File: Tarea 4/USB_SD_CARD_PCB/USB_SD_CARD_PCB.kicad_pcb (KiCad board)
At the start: 2 copper layers, 54.8 x 37.1 mm, 3 parts

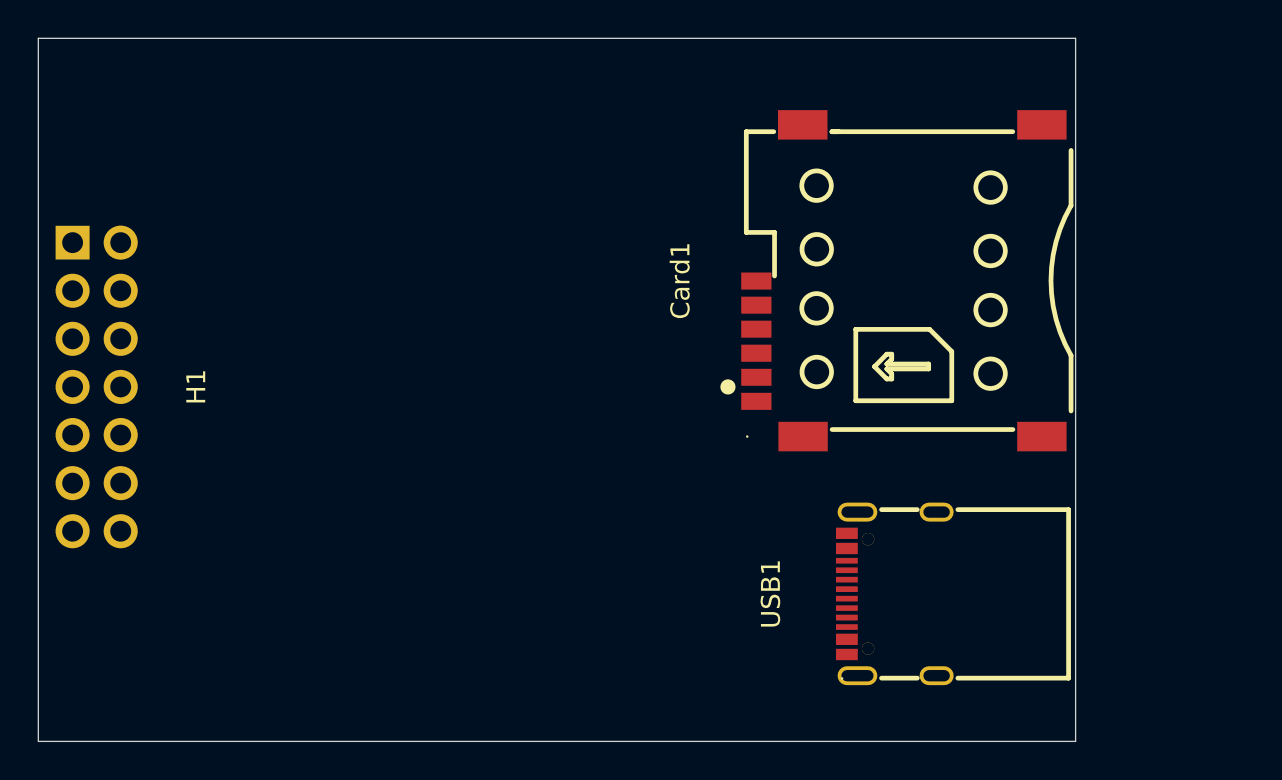
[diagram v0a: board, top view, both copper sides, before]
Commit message: USB type c Conexiones
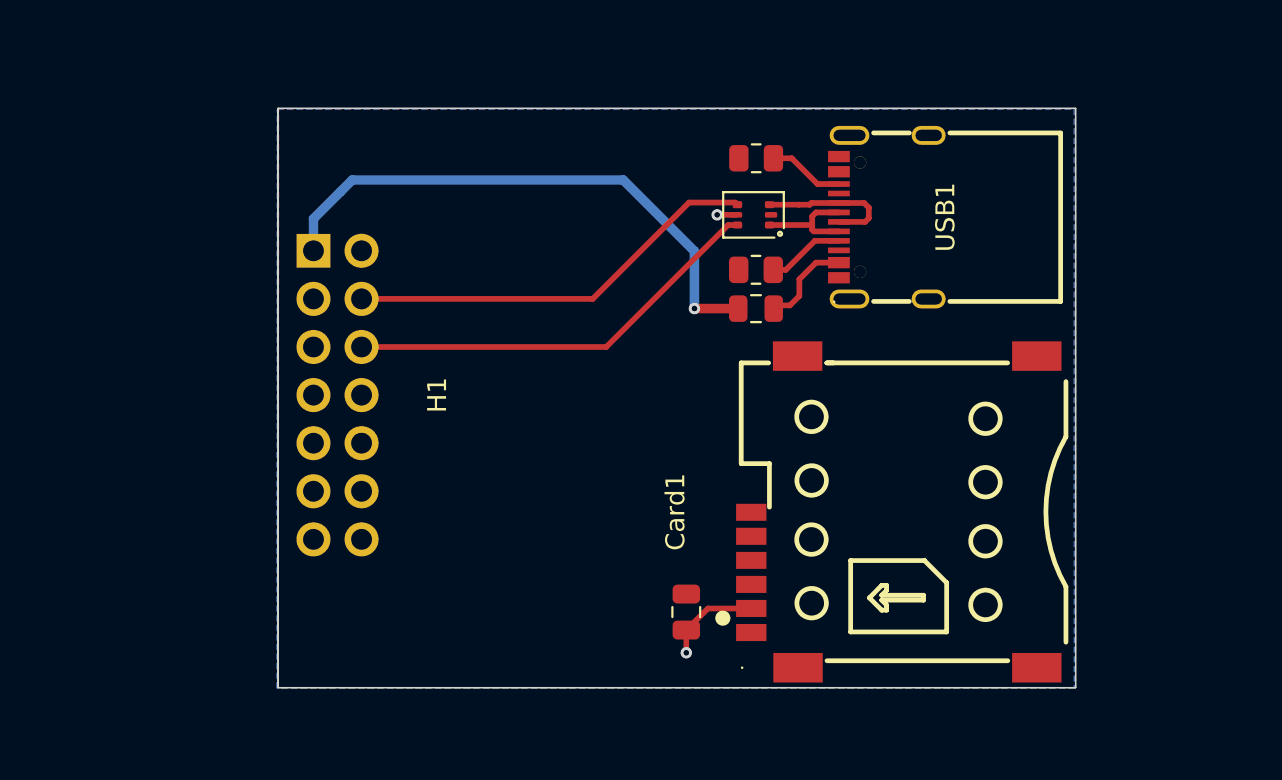
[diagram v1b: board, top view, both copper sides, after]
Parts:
- added C3: 100nf, Capacitor_SMD:C_0805_2012Metric, F.Cu at (111.8, 95.1)
- added D1: USBLC6-2P6, PCM_Package_TO_SOT_SMD_AKL:SOT-666, F.Cu at (115.3, 74.2)
- added F1: Polyfuse_Small, Fuse:Fuse_0805_2012Metric, F.Cu at (115.5, 79.1)
- added R1: 5.1k, Resistor_SMD:R_0805_2012Metric, F.Cu at (115.5, 77.1)
- added R2: 5.1k, Resistor_SMD:R_0805_2012Metric, F.Cu at (115.5, 71.2)
- moved USB1 19.9 mm to (122.2, 74.3)
- moved H1 12.7 mm to (93.4, 83.7)
- moved Card1 12.2 mm to (122.8, 89.8)
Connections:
- Card1 pad 10: unconnected-(Card1-GND-Pad10) -> GND
- Card1 pad 7: unconnected-(Card1-GND-Pad7) -> GND
- Card1 pad 8: unconnected-(Card1-GND-Pad8) -> GND
- Card1 pad 9: unconnected-(Card1-GND-Pad9) -> GND
- Card1 pad C1: unconnected-(Card1-VCC-PadC1) -> +3.3V
- Card1 pad C3: unconnected-(Card1-CLK-PadC3) -> /clk
- Card1 pad C5: unconnected-(Card1-GND-PadC5) -> GND
- Card1 pad C7: unconnected-(Card1-I/O-PadC7) -> /GPIO1
- H1 pad 1: unconnected-(H1-Pad1) -> +5V
- H1 pad 10: unconnected-(H1-Pad10) -> /i2c_scl
- H1 pad 11: unconnected-(H1-Pad11) -> /GPIO1
- H1 pad 12: unconnected-(H1-Pad12) -> /GPIO2
- H1 pad 13: unconnected-(H1-Pad13) -> GND
- H1 pad 14: unconnected-(H1-Pad14) -> GND
- H1 pad 2: unconnected-(H1-Pad2) -> +3.3V
- H1 pad 3: unconnected-(H1-Pad3) -> /cs
- H1 pad 4: unconnected-(H1-Pad4) -> /usb+
- H1 pad 5: unconnected-(H1-Pad5) -> /mosi
- H1 pad 6: unconnected-(H1-Pad6) -> /usb-
- H1 pad 7: unconnected-(H1-Pad7) -> /miso
- H1 pad 8: unconnected-(H1-Pad8) -> /i2c_sda
- H1 pad 9: unconnected-(H1-Pad9) -> /clk
- USB1 pad A5: unconnected-(USB1-CC1-PadA5) -> Net-(USB1-CC1)
- USB1 pad A6: unconnected-(USB1-DP1-PadA6) -> /D+
- USB1 pad A7: unconnected-(USB1-DN1-PadA7) -> /D-
- USB1 pad B5: unconnected-(USB1-CC2-PadB5) -> Net-(USB1-CC2)
- USB1 pad B6: unconnected-(USB1-DP2-PadB6) -> /D+
- USB1 pad B7: unconnected-(USB1-DN2-PadB7) -> /D-
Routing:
- net +5V: track 0.00 -> 29.6 mm, vias 0 -> 1
- net /usb-: track 0.00 -> 22.5 mm
- net /usb+: track 0.00 -> 22.0 mm
- net /D+: track 0.00 -> 7.59 mm
- net +3.3V: track 0.00 -> 6.10 mm, vias 0 -> 2
- net /D-: track 0.00 -> 5.92 mm
- net Net-(F1-Pad2): track 0.00 -> 4.96 mm
- net Net-(USB1-CC1): track 0.00 -> 4.10 mm
- net Net-(USB1-CC2): track 0.00 -> 4.02 mm
- added copper zone on B.Cu, net +3.3V
- added copper zone on F.Cu, net GND
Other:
- board size 54.8 x 37.1 mm -> 42.1 x 30.6 mm

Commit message: USB CARD Y SD
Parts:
- removed Card1: SMC-202-6, EasyEDA:SIM-SMD_SMC-202-6
- removed H1: PZ254R-12-14P, EasyEDA:HDR-TH_14P-P2.54-H-M-R2-C7-S2.54
- added C1: 100nf, Capacitor_SMD:C_0805_2012Metric, F.Cu at (118.0, 82.8)
- added Card2: TF-115, EasyEDA:TF-SMD_TF-115, F.Cu at (128.8, 89.3)
- added FPC1: FPC-05FB-30PH20, EasyEDA:FPC-SMD_30P-P0.50_FPC-05FB-30PH20, F.Cu at (109.1, 84.0)
- added J1: PZ254R-12-16P, EasyEDA:HDR-TH_16P-P2.54-H-M-R2-C8-S2.54, F.Cu at (99.1, 84.1)
- added R3: 10k, Resistor_SMD:R_0805_2012Metric, F.Cu at (118.0, 85.1)
- added R4: 10k, Resistor_SMD:R_0805_2012Metric, F.Cu at (118.0, 88.1)
- added R5: 10k, Resistor_SMD:R_0805_2012Metric, F.Cu at (118.0, 91.0)
- added R6: 10k, Resistor_SMD:R_0805_2012Metric, F.Cu at (118.0, 94.0)
- moved USB1 7.49 mm to (129.7, 74.2)
- moved R1 6.91 mm to (122.3, 76.0)
- moved F1 6.91 mm to (122.3, 78.0)
- moved R2 6.91 mm to (122.3, 70.1)
- moved D1 6.91 mm to (122.2, 73.1)
- moved C3 6.43 mm to (118.1, 96.5), turned to 0 degrees
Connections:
- D1 pad 4: /usb+ -> /USB+
- D1 pad 6: /usb- -> /USB-
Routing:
- net +5V: track 29.6 -> 0.00 mm, vias 1 -> 0
- net /usb-: track 22.5 -> 0.00 mm
- net /usb+: track 22.0 -> 0.00 mm
- net /D+: track 7.59 -> 0.00 mm
- net +3.3V: track 6.10 -> 0.00 mm, vias 2 -> 0
- net /D-: track 5.92 -> 0.00 mm
- net Net-(F1-Pad2): track 4.96 -> 0.00 mm
- net Net-(USB1-CC1): track 4.10 -> 0.00 mm
- net Net-(USB1-CC2): track 4.02 -> 0.00 mm
- removed copper zone on B.Cu, net +3.3V
- removed copper zone on F.Cu, net GND
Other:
- board size 42.1 x 30.6 mm -> 42.4 x 32.3 mm
- copper layers 2 -> 4

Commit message: Actualizacion 18/04/26
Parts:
- added C2: 10uF, Capacitor_SMD:C_0201_0603Metric, F.Cu at (113.6, 93.0)
- added R10: 10K, PCM_Resistor_SMD_AKL:R_0603_1608Metric, F.Cu at (115.5, 91.0)
- added R11: 10K, PCM_Resistor_SMD_AKL:R_0603_1608Metric, F.Cu at (115.5, 89.1)
- added R7: 6.8K, PCM_Resistor_SMD_AKL:R_0603_1608Metric, F.Cu at (116.0, 97.2)
- added R8: 300R, PCM_Resistor_SMD_AKL:R_0603_1608Metric, F.Cu at (112.2, 95.4)
- added R9: 10K, PCM_Resistor_SMD_AKL:R_0603_1608Metric, F.Cu at (115.5, 87.1)
- added U1: MT9700-N, EasyEDA:SOT-23-5_L2.9-W1.6-P0.95-LS2.9-BL, F.Cu at (116.0, 94.3)
- R3, R4, R5, R6: footprint Resistor_SMD:R_0805_2012Metric -> PCM_Resistor_SMD_AKL:R_0603_1608Metric
- moved C3 28.1 mm to (126.1, 69.6)
- moved R5 5.03 mm to (120.3, 95.5)
- moved D1 4.26 mm to (126.3, 74.0)
- moved R2 4.21 mm to (126.2, 71.6)
- moved F1 4.07 mm to (126.3, 78.4)
- moved R1 4.07 mm to (126.3, 76.3)
- moved C1 2.48 mm to (120.3, 82.1)
- moved R3 2.48 mm to (120.4, 84.4)
- moved R4 2.48 mm to (120.4, 87.4)
- moved R6 2.30 mm to (120.3, 93.7)
- moved USB1 2.10 mm to (131.8, 74.3)
- moved Card2 1.92 mm to (130.7, 89.2)
- moved FPC1 0.95 mm to (110.0, 84.0), turned to -90 degrees
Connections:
- FPC1 pad 1: unconnected-(FPC1-Pad1) -> GND
- FPC1 pad 2: unconnected-(FPC1-Pad2) -> VDD
- FPC1 pad 20: unconnected-(FPC1-Pad20) -> /LED+
- FPC1 pad 21: unconnected-(FPC1-Pad21) -> GND
- FPC1 pad 22: unconnected-(FPC1-Pad22) -> GND
- FPC1 pad 23: unconnected-(FPC1-Pad23) -> GND
- FPC1 pad 24: unconnected-(FPC1-Pad24) -> GND
- FPC1 pad 25: unconnected-(FPC1-Pad25) -> +3.3V
- FPC1 pad 26: unconnected-(FPC1-Pad26) -> /I2C_SCK
- FPC1 pad 27: unconnected-(FPC1-Pad27) -> /I2C_SDA
- FPC1 pad 28: unconnected-(FPC1-Pad28) -> /TP_INT
- FPC1 pad 29: unconnected-(FPC1-Pad29) -> /RESET
- FPC1 pad 3: unconnected-(FPC1-Pad3) -> /IM2
- FPC1 pad 30: unconnected-(FPC1-Pad30) -> GND
- FPC1 pad 31: unconnected-(FPC1-Pad31) -> GND
- FPC1 pad 32: unconnected-(FPC1-Pad32) -> GND
- FPC1 pad 4: unconnected-(FPC1-Pad4) -> /IM1
- FPC1 pad 5: unconnected-(FPC1-Pad5) -> /RESET
- FPC1 pad 6: unconnected-(FPC1-Pad6) -> /LCD_CS
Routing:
- net +5V: track 0.00 -> 30.9 mm, vias 0 -> 1
- net /USB-: track 0.00 -> 29.5 mm, vias 0 -> 1
- net /USB+: track 0.00 -> 29.5 mm, vias 0 -> 1
- net +3.3V: track 0.00 -> 17.1 mm, vias 0 -> 18
- net Net-(F1-Pad2): track 0.00 -> 13.0 mm
- net Net-(Card2-DAT2): track 0.00 -> 5.17 mm
- net VDD: track 0.00 -> 5.15 mm
- net /D+: track 0.00 -> 5.11 mm
- net /D-: track 0.00 -> 5.00 mm
- net Net-(Card2-DAT1): track 0.00 -> 4.58 mm
- net /SD_CS: track 0.00 -> 4.40 mm
- net /SPI_MISO: track 0.00 -> 4.29 mm
- net /RESET: track 0.00 -> 3.89 mm
- net GND: track 0.00 -> 3.33 mm
- net /IM2: track 0.00 -> 3.31 mm
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- added copper zone on B.Cu, net +3.3V
- added copper zone on F.Cu, net +3.3V
- added copper zone on F.Cu, net GND
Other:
- board size 42.4 x 32.3 mm -> 44.2 x 32.3 mm
- board text added: "Made by José Daniel"
